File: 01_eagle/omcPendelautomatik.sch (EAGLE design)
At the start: 71 parts, among them IC1 PIC12F675, IC2 7805, IC3 L5970D, K1 NA-5V, T1 BSS138, T2 BSS138, X1 RT034 Typ 086, X2 2X3

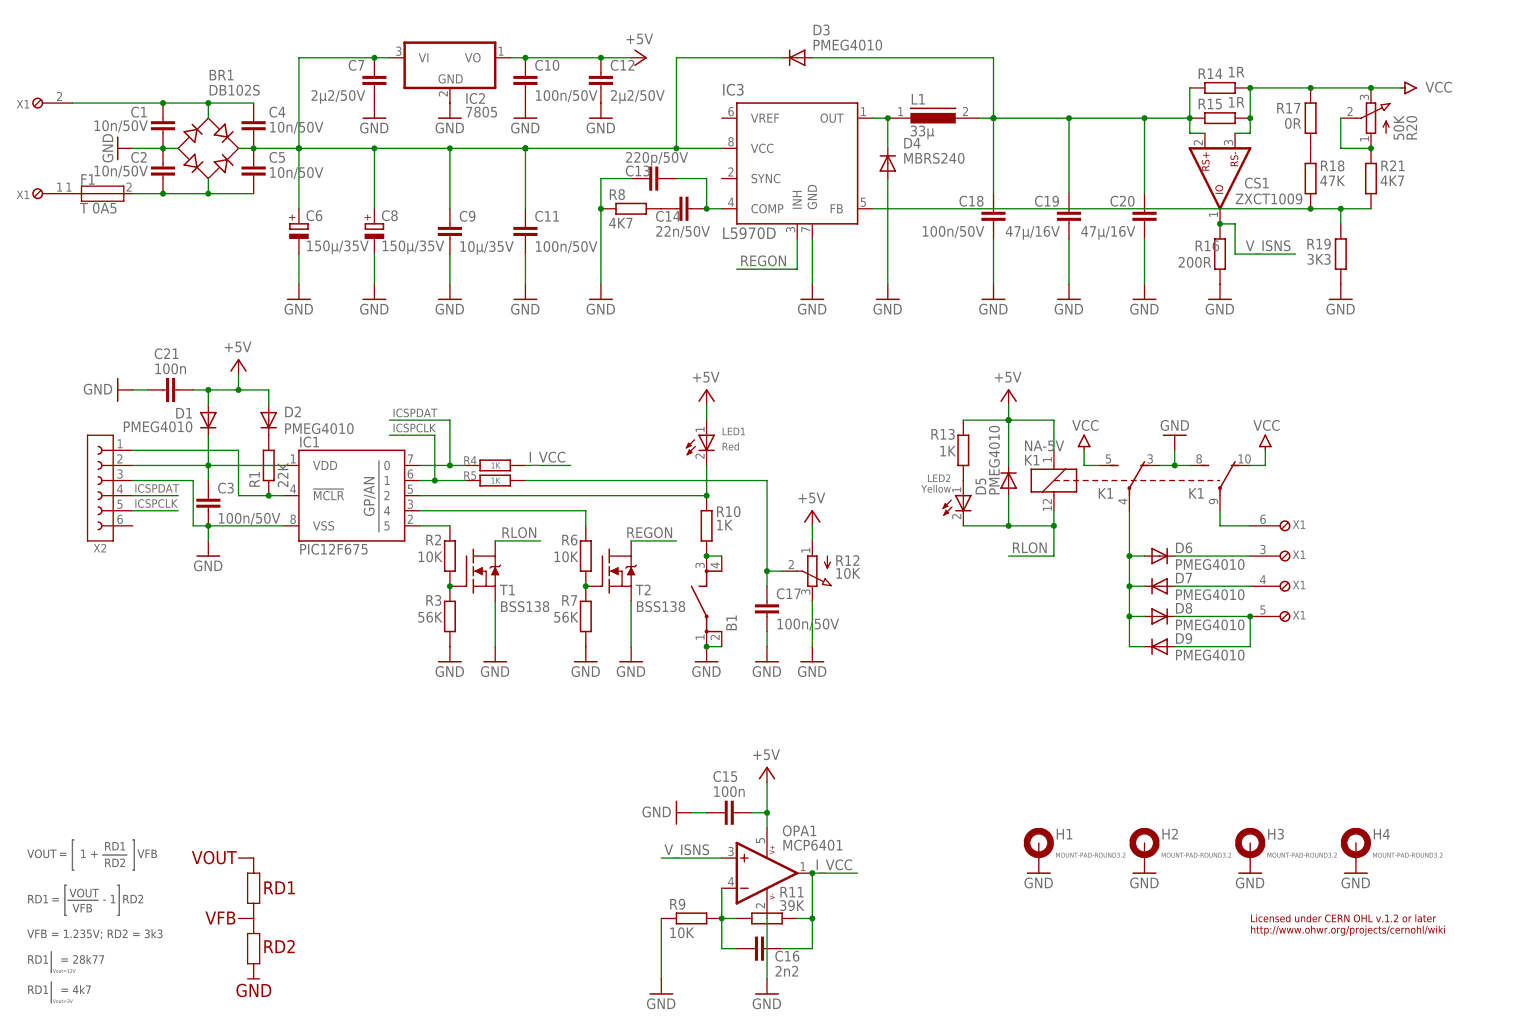
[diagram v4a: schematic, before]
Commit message: bugfix uC button wiring
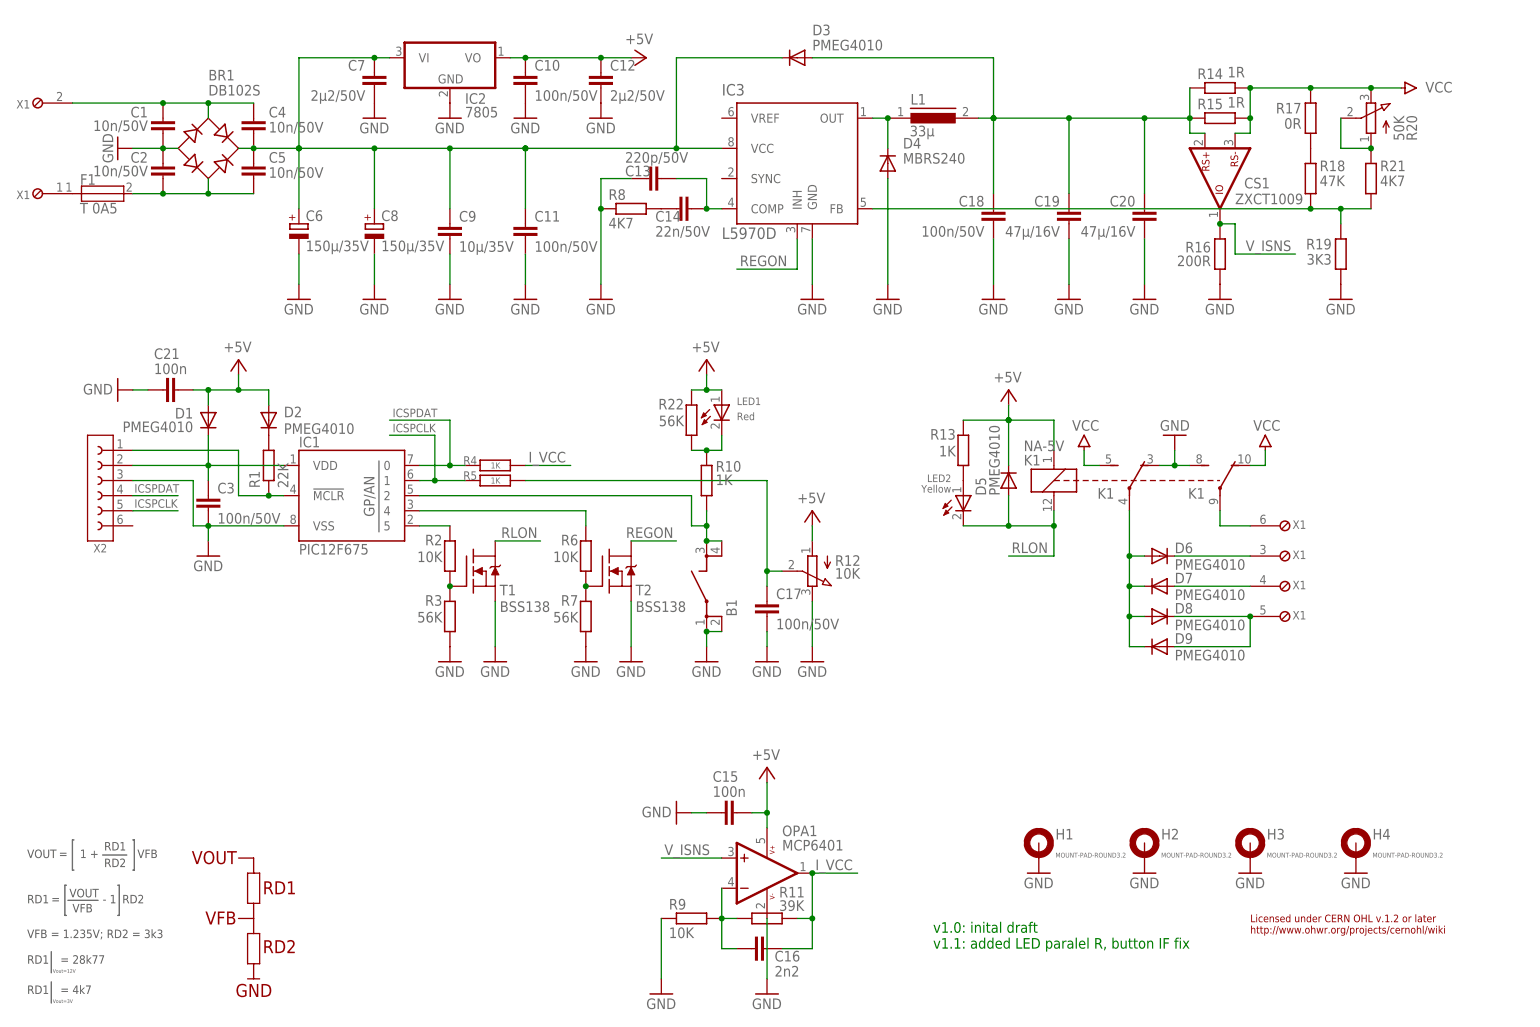
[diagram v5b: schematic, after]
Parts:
- added R22: 56K, omcResistor:RC1206-56000
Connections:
- removed net N$28: B1.P$3, B1.P$4, R10.1
- new net N$32: LED1.C, R10.2, R22.1
- net +5V: now also R22.2
- net N$27: now also B1.P$3, B1.P$4, R10.1; no longer LED1.C, R10.2
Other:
- note added: "v1.0: inital draft v1.1: added LED paralel R, button IF fix"
- moved on the sheet: B1, LED1, R10
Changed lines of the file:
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@@
 <setting verticaltext="up"/>
 </settings>
-<grid distance="0.1" unitdist="inch" unit="inch" style="lines" multiple="1" display="no" altdistance="0.01" altunitdist="inch" altunit="inch"/>
+<grid distance="0.1" unitdist="inch" unit="inch" style="lines" multiple="1" display="yes" altdistance="0.01" altunitdist="inch" altunit="inch"/>
 <layers>
 <layer number="1" name="Top" color="4" fill="1" visible="no" active="no"/>
@@
 <part name="C21" library="omcCapacitor" deviceset="X7R" device="-1206" technology="-100000P" value="100n"/>
 <part name="GND34" library="supply1" deviceset="GND" device=""/>
+<part name="R22" library="omcResistor" deviceset="RC1206" device="" technology="-56000" value="56K"/>
 </parts>
 <sheets>
@@
 <wire x1="24.638" y1="104.14" x2="20.32" y2="104.14" width="0.1524" layer="94"/>
 <text x="211.074" y="140.208" size="1.27" layer="98">V_ISNS [V] = I_VCC [A]</text>
-<text x="131.318" y="75.184" size="1.4224" layer="98" rot="R90">over-current
+<text x="131.318" y="77.724" size="1.4224" layer="98" rot="R90">over-current
 reset button</text>
+<text x="162.56" y="17.78" size="1.778" layer="91">v1.0: inital draft
+v1.1: added LED paralel R, button IF fix</text>
 </plain>
 <instances>
@@
 </instance>
 <instance part="R16" gate="G$1" x="210.82" y="134.62" smashed="yes" rot="R90">
-<attribute name="NAME" x="206.502" y="135.1026" size="1.778" layer="95"/>
-<attribute name="VALUE" x="203.708" y="132.334" size="1.778" layer="96"/>
+<attribute name="NAME" x="209.296" y="136.6774" size="1.778" layer="95" rot="R180"/>
+<attribute name="VALUE" x="209.296" y="134.366" size="1.778" layer="96" rot="R180"/>
 </instance>
 <instance part="GND30" gate="1" x="210.82" y="127"/>
@@
 <attribute name="VALUE" x="135.89" y="13.081" size="1.778" layer="96"/>
 </instance>
-<instance part="LED1" gate="G$1" x="124.46" y="101.6"/>
-<instance part="R10" gate="G$1" x="124.46" y="88.9" smashed="yes" rot="R90">
-<attribute name="NAME" x="125.984" y="90.3986" size="1.778" layer="95"/>
-<attribute name="VALUE" x="125.984" y="88.138" size="1.778" layer="96"/>
-</instance>
-<instance part="P+3" gate="1" x="124.46" y="111.76" smashed="yes">
-<attribute name="VALUE" x="121.92" y="113.03" size="1.778" layer="96"/>
+<instance part="LED1" gate="G$1" x="127" y="106.68"/>
+<instance part="R10" gate="G$1" x="124.46" y="96.52" smashed="yes" rot="R90">
+<attribute name="NAME" x="125.984" y="98.0186" size="1.778" layer="95"/>
+<attribute name="VALUE" x="125.984" y="95.758" size="1.778" layer="96"/>
+</instance>
+<instance part="P+3" gate="1" x="124.46" y="116.84" smashed="yes">
+<attribute name="VALUE" x="121.92" y="118.11" size="1.778" layer="96"/>
 </instance>
 <instance part="H1" gate="G$1" x="180.34" y="35.56" smashed="yes" rot="R90">
@@
 </instance>
 <instance part="GND33" gate="1" x="233.68" y="30.48"/>
-<instance part="B1" gate="G$1" x="127" y="76.2" rot="R90"/>
+<instance part="B1" gate="G$1" x="127" y="78.74" rot="R90"/>
 <instance part="GND18" gate="1" x="124.46" y="66.04"/>
 <instance part="C15" gate="G$1" x="127" y="40.64" smashed="yes" rot="R90">
@@
 <instance part="GND34" gate="1" x="25.4" y="111.76" smashed="yes" rot="R270">
 <attribute name="VALUE" x="19.558" y="110.998" size="1.778" layer="96"/>
+</instance>
+<instance part="R22" gate="G$1" x="121.92" y="106.68" smashed="yes" rot="R90">
+<attribute name="NAME" x="120.65" y="110.2614" size="1.778" layer="95" rot="R180"/>
+<attribute name="VALUE" x="120.65" y="107.442" size="1.778" layer="96" rot="R180"/>
 </instance>
 </instances>
@@
 <pinref part="B1" gate="G$1" pin="P$2"/>
 <pinref part="B1" gate="G$1" pin="P$1"/>
-<wire x1="127" y1="68.58" x2="124.46" y2="68.58" width="0.1524" layer="91"/>
+<wire x1="127" y1="71.12" x2="124.46" y2="71.12" width="0.1524" layer="91"/>
 <pinref part="GND18" gate="1" pin="GND"/>
-<junction x="124.46" y="68.58"/>
+<junction x="124.46" y="71.12"/>
+<wire x1="124.46" y1="71.12" x2="124.46" y2="68.58" width="0.1524" layer="91"/>
 </segment>
 <segment>
@@
 <pinref part="P+3" gate="1" pin="+5V"/>
 <pinref part="LED1" gate="G$1" pin="A"/>
-<wire x1="124.46" y1="109.22" x2="124.46" y2="106.68" width="0.1524" layer="91"/>
+<pinref part="R22" gate="G$1" pin="2"/>
+<wire x1="121.92" y1="111.76" x2="124.46" y2="111.76" width="0.1524" layer="91"/>
+<wire x1="124.46" y1="111.76" x2="127" y2="111.76" width="0.1524" layer="91"/>
+<wire x1="124.46" y1="114.3" x2="124.46" y2="111.76" width="0.1524" layer="91"/>
+<junction x="124.46" y="111.76"/>
 </segment>
 </net>
@@
 <segment>
 <pinref part="IC1" gate="G$1" pin="2"/>
-<wire x1="76.2" y1="93.98" x2="124.46" y2="93.98" width="0.1524" layer="91"/>
-<pinref part="R10" gate="G$1" pin="2"/>
-<wire x1="124.46" y1="93.98" x2="124.46" y2="99.06" width="0.1524" layer="91"/>
-<junction x="124.46" y="93.98"/>
-<pinref part="LED1" gate="G$1" pin="C"/>
-</segment>
-</net>
-<net name="N$28" class="0">
-<segment>
+<wire x1="76.2" y1="93.98" x2="121.92" y2="93.98" width="0.1524" layer="91"/>
+<wire x1="121.92" y1="93.98" x2="121.92" y2="88.9" width="0.1524" layer="91"/>
 <pinref part="R10" gate="G$1" pin="1"/>
 <pinref part="B1" gate="G$1" pin="P$3"/>
 <pinref part="B1" gate="G$1" pin="P$4"/>
-<wire x1="127" y1="83.82" x2="124.46" y2="83.82" width="0.1524" layer="91"/>
-<junction x="124.46" y="83.82"/>
+<wire x1="124.46" y1="91.44" x2="124.46" y2="88.9" width="0.1524" layer="91"/>
+<wire x1="124.46" y1="88.9" x2="124.46" y2="86.36" width="0.1524" layer="91"/>
+<wire x1="124.46" y1="86.36" x2="127" y2="86.36" width="0.1524" layer="91"/>
+<junction x="124.46" y="86.36"/>
+<wire x1="121.92" y1="88.9" x2="124.46" y2="88.9" width="0.1524" layer="91"/>
+<junction x="124.46" y="88.9"/>
 </segment>
 </net>
@@
 </segment>
 </net>
+<net name="N$32" class="0">
+<segment>
+<pinref part="LED1" gate="G$1" pin="C"/>
+<pinref part="R10" gate="G$1" pin="2"/>
+<pinref part="R22" gate="G$1" pin="1"/>
+<wire x1="121.92" y1="101.6" x2="124.46" y2="101.6" width="0.1524" layer="91"/>
+<junction x="124.46" y="101.6"/>
+<wire x1="124.46" y1="101.6" x2="127" y2="101.6" width="0.1524" layer="91"/>
+<wire x1="127" y1="101.6" x2="127" y2="104.14" width="0.1524" layer="91"/>
+</segment>
+</net>

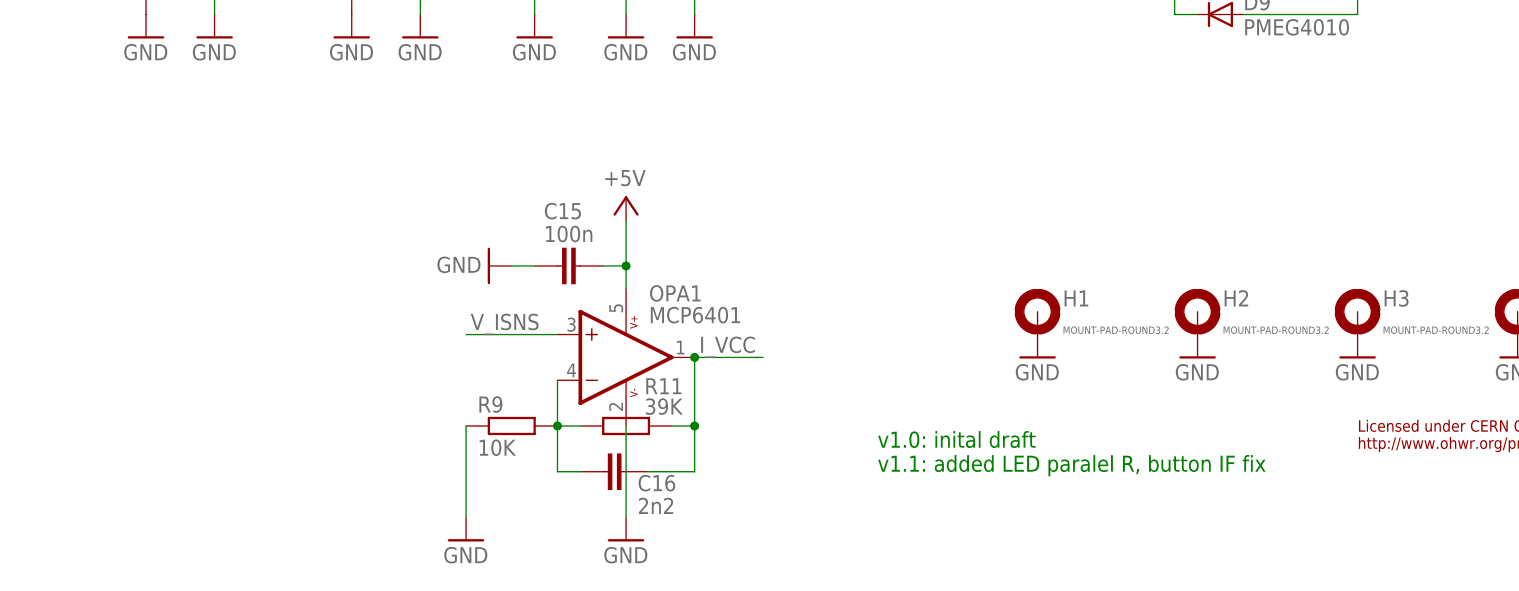
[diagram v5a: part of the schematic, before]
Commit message: omcPendelautomatik.sch -> added tank capacitor for current sense adc
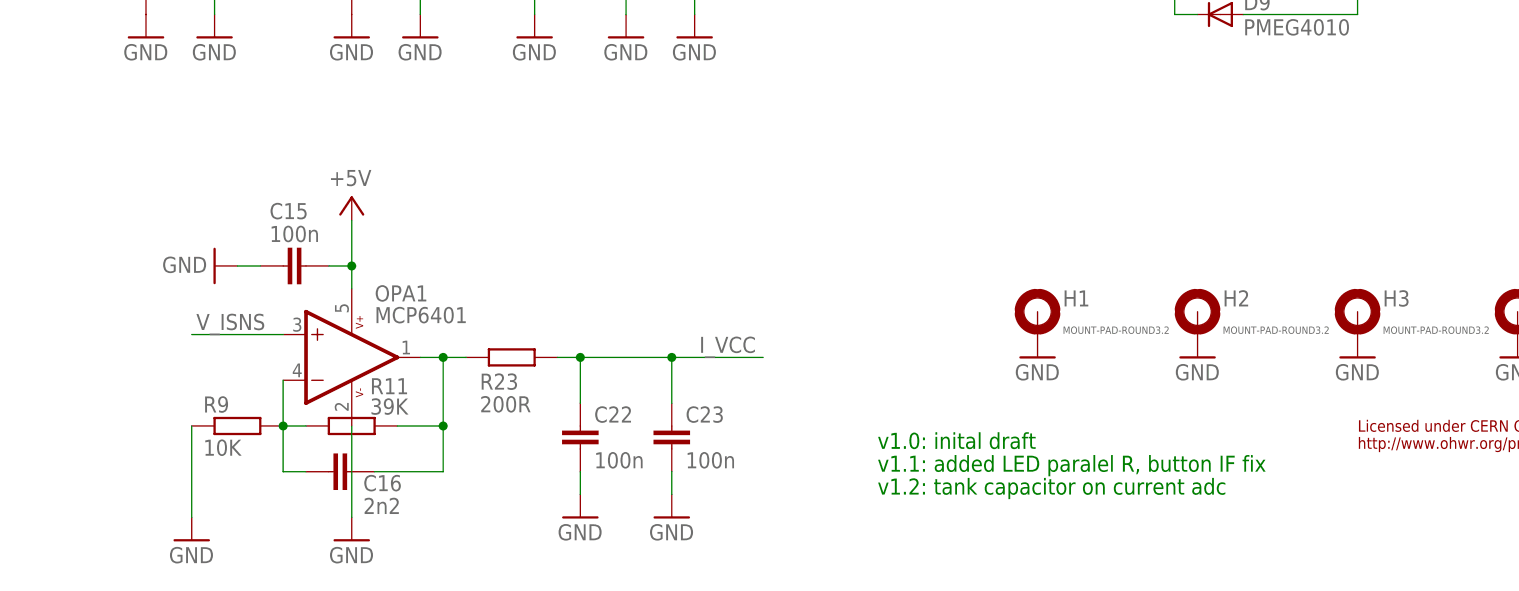
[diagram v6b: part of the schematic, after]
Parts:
- added C22, C23: 100n, omcCapacitor:X7R-100000P-1206
- added R23: 200R, omcResistor:RC1206-200
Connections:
- new net N$33: C16.2, OPA1G$1.OUT, R11.2, R23.2
- net GND: now also C22.2, C23.2
- net I_VCC: now also C22.1, C23.1, R23.1; no longer C16.2, OPA1G$1.OUT, R11.2
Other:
- note added: "tank capacitor for adc"
- note added: "v1.0: inital draft"
- note added: "v1.1: added LED paralel R, button IF fix"
- note added: "v1.2: tank capacitor on current adc"
- note removed: "v1.0: inital draft v1.1: added LED paralel R, button IF fix"
- moved on the sheet: C15, C16, OPA1, R11, R9
